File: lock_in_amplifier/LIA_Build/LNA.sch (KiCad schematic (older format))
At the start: 15 parts, among them J38 RF_Shield_One_Piece, U5 NC7SB3157, U6 NC7SB3157, U7 NC7SB3157, U8 AD8429

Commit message: power supply, amp chain first pass
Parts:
- removed C22: C, Capacitors_SMD:C_0805_HandSoldering, symbol C
- removed L8: L, Inductors_SMD:L_0805_HandSoldering, symbol L
- removed R16, R17, R18, R19, R20: R, symbol R
- added J24: LNA GAIN MODE, symbol Conn_01x02
- C20, C21: footprint Capacitors_SMD:C_0805_HandSoldering -> Capacitors_SMD:C_0805
- J38: footprint (none) -> footprints:SMS-201
- R21: value R -> 6.04; footprint (none) -> Resistors_SMD:R_0805
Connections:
- wire segments 27 -> 26
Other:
- note added: "A OR I SELECTION SWITCH"
- note added: "A/I OR A-B SELECTION SWITCH"
- note added: "AD8429 GAIN SELECTION VALUES (FROM DATASHEET)\n1x - open\n2x - 6.04k\n5x - 1.5k\n10x - 665 (2k||2k||2k)\n20x - 316\n50x - 121\n100x - 60.4 (121||121)\n1000x - 6.04"
- note added: "GAIN SELECTION SWITCH"
- note added: "GAIN SELECTION. INPUT LNA HAS 1 V/V (BUFFER MODE)\nOR 1000 V/V GAIN (LNA MODE).\nTHIS MINIMIZES "WEIRD" RESISTOR VALUE QUANTITIES.\nALSO REDUCES SIZE OF SWITCH BLOCK FOR EMI CONCERNS"
- note added: "INSTRUMENTATION AMPLIFIER SECTION\n"
- note added: "TRANSIMPEDANCE AMPLIFIER"
- note added: "◦ Transimpedance amp w/ switches for single ended, differential, and current inputs\n ◦ Nominal goal for 1 nV sensitivity with long enough time base; 1nV -> ~1V\n ▪ 1e9 v/v system gain.\n • Line filter at input - concerns with saturation\n\n"
- note removed: "A or I selection"
- note removed: "A/I or A-B selection"
- note removed: "INSTRUMENTATION AMPLIFIER SECTION\nNOTE: AD8428 (FIXED GAIN INST. AMP.) SUBSTITUTABLE BY REMOVING Rg"
- note removed: "TODO: line filter - 60Hz"
- note removed: "TODO: verify which resistors I have in stock\nminimaze part count\n1x - open\n2x - 6.04k\n5x - 1.5k\n10x - 665 (2k||2k||2k)\n20x - 316\n50x - 121\n100x - 60.4 (121||121)"
- note removed: "dip switch?"
- note removed: "gain selection block"
- note removed: "transimpedance amplifier"
- note removed: "◦ Transimpedance amp w/ switches for single ended, differential, and current inputs\n ▪ Component selection\n ▪ Switches - spdt\n ◦ Switched gain \n ▪ common numbers for measurement (1x one of the amps)\n ▪ Switch selection\n ▪ 2xN 100 mil header jumpers\n ▪ N pole N throw slide switch - $$$? Real estate?\n ▪ DIP\n • 2 amp cascade - LNA + “normal” amp\n ◦ Nominal goal for 1 nV sensitivity with lo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"
- moved on the sheet: C20, C21, J38, R21, U8

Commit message: initial transimpedance selection, lna refinement
amp overload led
switch comps added
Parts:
- removed J24: LNA GAIN MODE, symbol Conn_01x02
- removed U5, U6, U7: NC7SB3157, symbol NC7SB3157
- added C25, C27: 10pF, symbol C
- added C34, C35, C37, C38: 0.1u, Capacitors_SMD:C_0805, symbol C
- added C36, C39: C, symbol C
- added J17: RF_Shield_One_Piece, footprints:SMS-201, symbol RF_Shield_One_Piece
- added R46: 10k, symbol R
- added R47, R58: 100, symbol R
- added R48, R55: 1M, symbol R
- added R49, R50: 10M, symbol R
- added R56, R57: 0, symbol R
- added R59: R, symbol R
- added R60: 10, symbol R
- added S4: A / I SEL, symbol SPDT
- added S5: B SEL, symbol SPDT
- added S6: LNA GAIN SEL, symbol SPDT
- added U6: lmp7721, Housings_SSOP:MSOP-8-1EP_3x3mm_Pitch0.65mm, symbol lmp7721
- added U7: OP1177, Housings_SSOP:MSOP-8-1EP_3x3mm_Pitch0.65mm, symbol OP1177
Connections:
- wire segments 26 -> 78
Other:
- note added: "AD8429 GAIN SELECTION VALUES (FROM DATASHEET)\n1x - open\n2x - 6.04k\n5x - 1.5k\n10x - 665 (2k||2k||2k)\n20x - 316\n50x - 121\n100x - 60.4 (121||121)\n1000x - 6.04\nGAIN SELECTION. INPUT LNA HAS 1 V/V (BUFFER MODE)\nOR 1000 V/V GAIN (LNA MODE).\nTHIS MINIMIZES "WEIRD" RESISTOR VALUE QUANTITIES."
- note added: "CONSIDER 6.04 (OR 2X 6.04) FOR RG TO REDUCE PART COUNT"
- note added: "DETERMINE FEED BACK AND LOOP BW"
- note added: "DETERMINE FEEDBACK RESISTANCE\nDETERMINE LOOP BW"
- note added: "DETERMINE POTENTIAL FOR THIS CAN."
- note added: "DETERMINE Rgd VALUE"
- note added: "DNI"
- note added: "GAIN SELECTION SWITCH\nFULL OUTPUT OR DIV/1000\n10k || 1M = 9.901k"
- note added: "GUARD DRIVER"
- note added: "LAYOUT GUIDELINE: GUARD TRACE \nMUST SURROUND CURRENT INPUT TRACE\nREMOVE SOLDER MASK FROM INSIDE GUARD TRACE\nCAN SHOULD COMPOSE GUARD TRACE WHERE POSSIBLE"
- note added: "LAYOUT: \nPLACE GND/REF FB TERMINAL\nOUTSIDE GUARD AREA"
- note added: "LNA INSTRUMENTATION AMP"
- note added: "◦ Transimpedance amp w/ switches for single ended, differential, and current inputs\n ◦ Nominal goal for 1 nV sensitivity with long enough time base; 1nV -> ~1V\n ▪ 1e9 v/v system gain.\n • Line filter at output - concerns with saturation on high gain amp, not lna\n\n"
- note removed: "AD8429 GAIN SELECTION VALUES (FROM DATASHEET)\n1x - open\n2x - 6.04k\n5x - 1.5k\n10x - 665 (2k||2k||2k)\n20x - 316\n50x - 121\n100x - 60.4 (121||121)\n1000x - 6.04"
- note removed: "DNI - leave off unless neccesary\ncover input of LNA"
- note removed: "GAIN SELECTION SWITCH"
- note removed: "GAIN SELECTION. INPUT LNA HAS 1 V/V (BUFFER MODE)\nOR 1000 V/V GAIN (LNA MODE).\nTHIS MINIMIZES "WEIRD" RESISTOR VALUE QUANTITIES.\nALSO REDUCES SIZE OF SWITCH BLOCK FOR EMI CONCERNS"
- note removed: "INSTRUMENTATION AMPLIFIER SECTION\n"
- note removed: "◦ Transimpedance amp w/ switches for single ended, differential, and current inputs\n ◦ Nominal goal for 1 nV sensitivity with long enough time base; 1nV -> ~1V\n ▪ 1e9 v/v system gain.\n • Line filter at input - concerns with saturation\n\n"
- moved on the sheet: C20, C21, J38, R21, U8

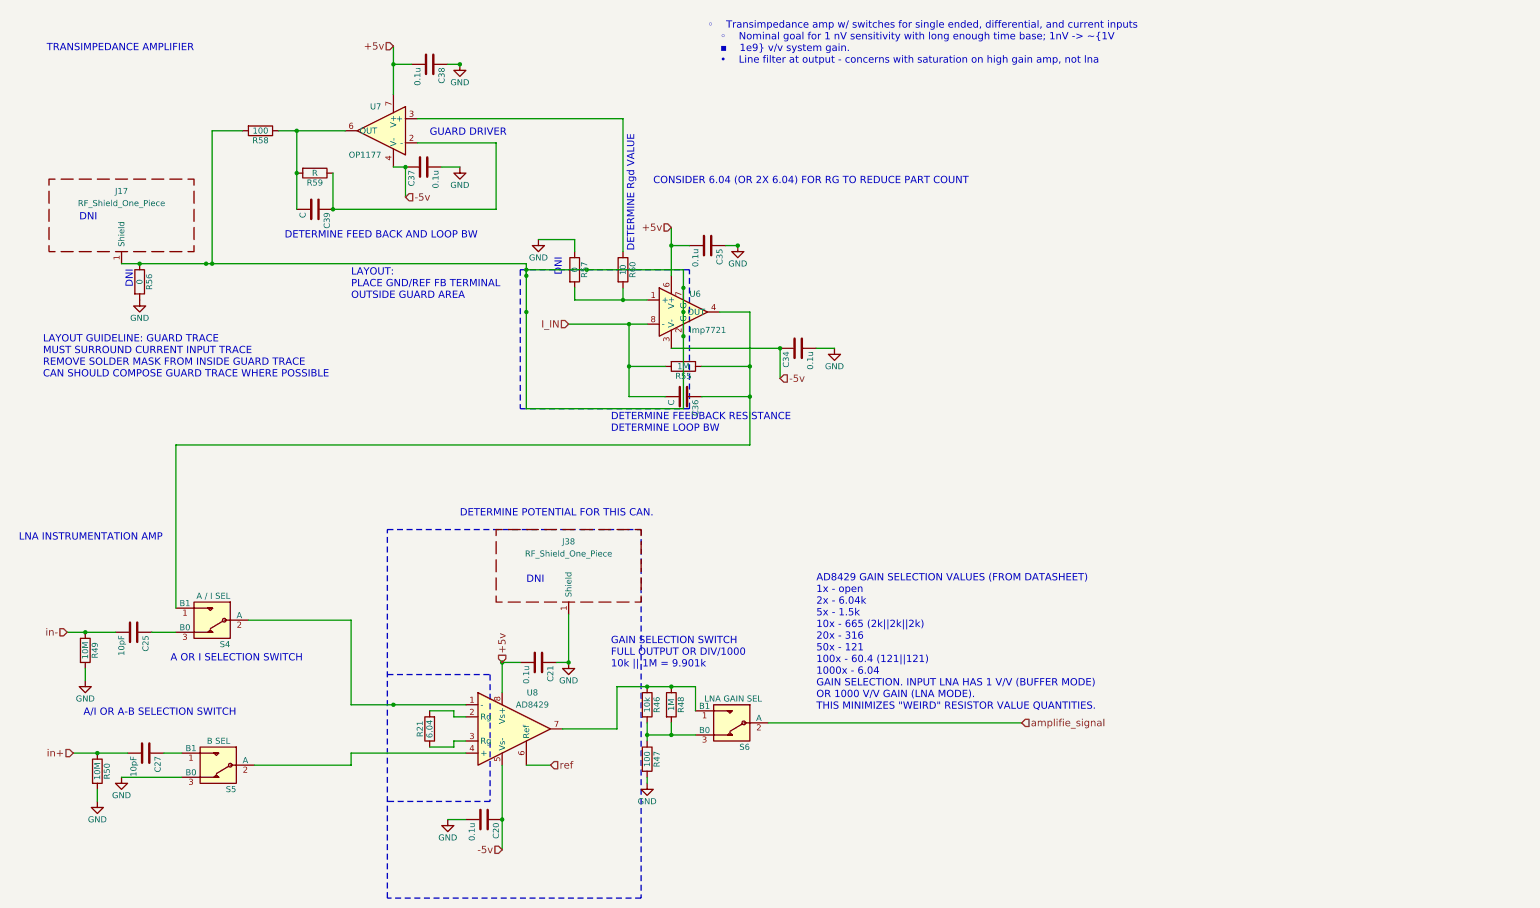
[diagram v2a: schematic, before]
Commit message: switch footprints, lm833 usage, pll investigation
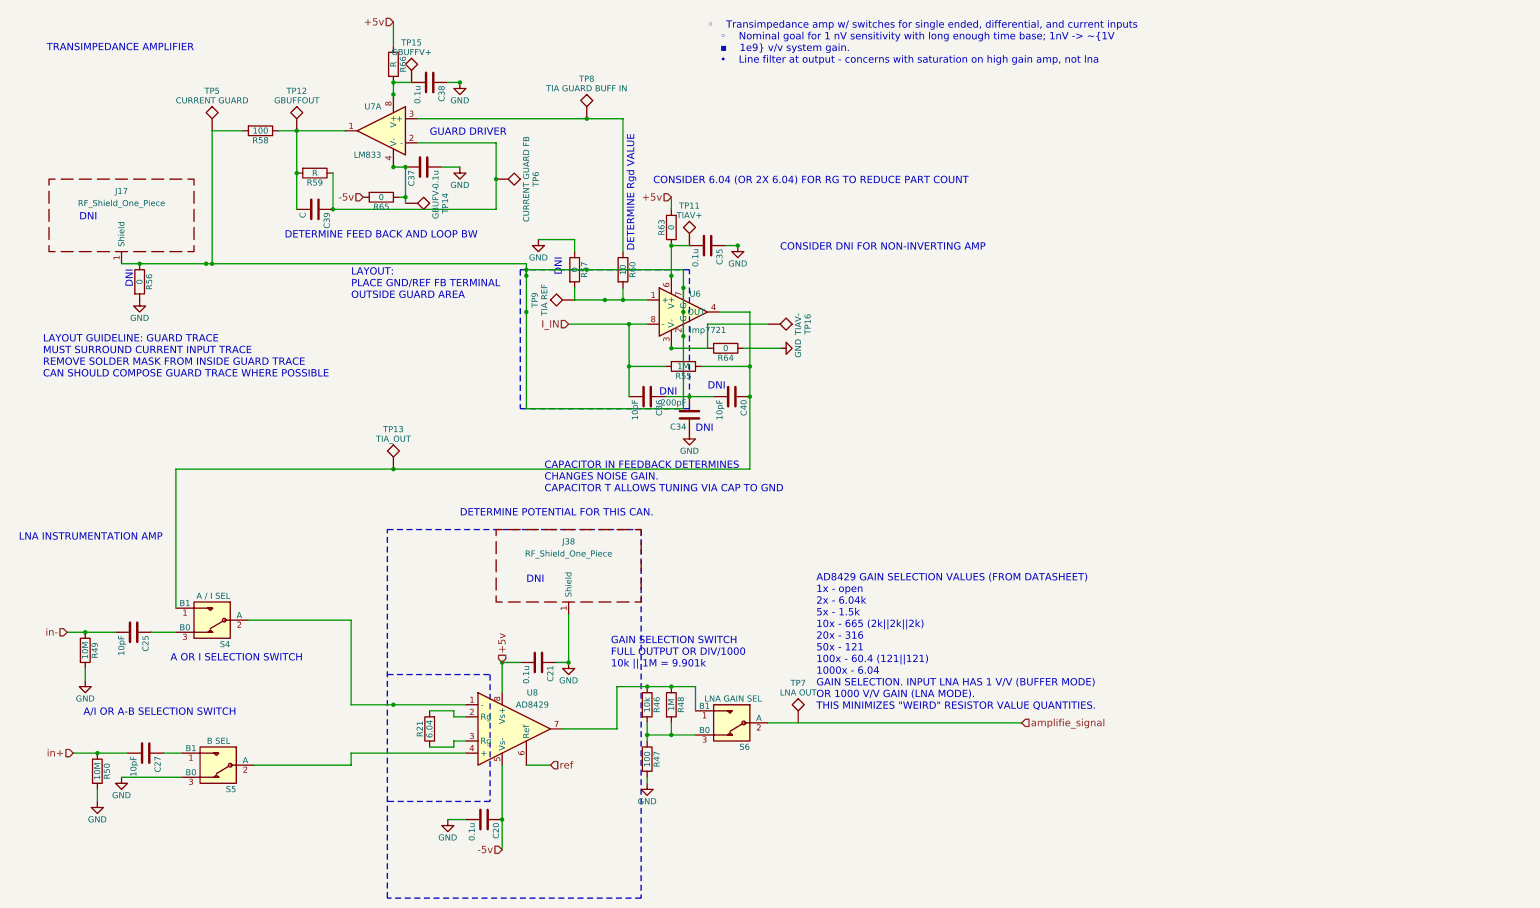
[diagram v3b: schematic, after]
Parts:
- removed U7: OP1177, Housings_SSOP:MSOP-8-1EP_3x3mm_Pitch0.65mm, symbol OP1177
- added C40: 10pF, symbol C
- added R63, R64, R65: 0, symbol R
- added R66: R, symbol R
- added TP11: TIAV+, symbol TEST
- added TP12: GBUFFOUT, symbol TEST
- added TP13: TIA_OUT, symbol TEST
- added TP14: GBUFV-, symbol TEST
- added TP15: GBUFFV+, symbol TEST
- added TP16: TIAV-, symbol TEST
- added TP5: CURRENT GUARD, symbol TEST
- added TP6: CURRENT GUARD FB, symbol TEST
- added TP7: LNA OUT, symbol TEST
- added TP8: TIA GUARD BUFF IN, symbol TEST
- added TP9: TIA REF, symbol TEST
- added U7: LM833, symbol LM833
- C34: value 0.1u -> 200pF; footprint Capacitors_SMD:C_0805 -> (none)
- C36: value C -> 10pF
- S4, S5, S6: footprint (none) -> footprints:SPDT_OS102011MS2QN1
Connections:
- net +5v: now also R63.2, R66.1; no longer C35.2, C38.2, U6.6 (V+)
- net -5v: now also R65.2; no longer C34.1, C37.1, U6.3 (V-)
- net GND: now also C34.1, R64.1; no longer C34.2
- net at R55.1, S4.1 (B1), U6.4 (OUT): now also C40.1, TP13.1; no longer C36.1
- net at J17.1 (Shield), R56.1, R58.2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: now also TP5.1
- net at C39.1, R59.1: now also TP6.1, U7.2 (-)
- net at R60.1: now also TP8.1, U7.3 (+)
- net at C39.2, R58.1, R59.2: now also TP12.1, U7.1
- net at R57.2, R60.2, U6.1 (+): now also TP9.1
- new net: C35.2, R63.1, TP11.1, U6.6 (V+)
- new net: C34.2, C36.1, C40.2
- new net: C38.2, R66.2, TP15.1, U7.8 (V+)
- new net: C37.1, R65.1, TP14.1, U7.4 (V-)
- new net: R64.2, TP16.1, U6.3 (V-)
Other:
- note added: "CAPACITOR IN FEEDBACK DETERMINES \nCHANGES NOISE GAIN.\nCAPACITOR T ALLOWS TUNING VIA CAP TO GND"
- note added: "CONSIDER DNI FOR NON-INVERTING AMP"
- note removed: "DETERMINE FEEDBACK RESISTANCE\nDETERMINE LOOP BW"
- moved on the sheet: C36, C38

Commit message: pll finalized - misc cleanup - review candidate
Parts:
- R60: value 10 -> 10K
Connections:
- net amplifie_signal: now also TP7.1
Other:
- note added: "◦ Transimpedance amp w/ switches for single ended, differential, and current inputs\n ◦ Nominal goal for 1 nV sensitivity with long enough time base; 1nV -> ~1V\n ▪ 1e9 v/v system gain.\n\n"
- note removed: "CONSIDER 6.04 (OR 2X 6.04) FOR RG TO REDUCE PART COUNT"
- note removed: "CONSIDER DNI FOR NON-INVERTING AMP"
- note removed: "DETERMINE POTENTIAL FOR THIS CAN."
- note removed: "DETERMINE Rgd VALUE"
- note removed: "◦ Transimpedance amp w/ switches for single ended, differential, and current inputs\n ◦ Nominal goal for 1 nV sensitivity with long enough time base; 1nV -> ~1V\n ▪ 1e9 v/v system gain.\n • Line filter at output - concerns with saturation on high gain amp, not lna\n\n"
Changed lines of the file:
@@
 $EndComp
 $Comp
-L GND #PWR067
+L GND #PWR073
 U 1 1 5A1C75B0
 P 4100 7200
-F 0 "#PWR067" H 4100 6950 50  0001 C CNN
+F 0 "#PWR073" H 4100 6950 50  0001 C CNN
 F 1 "GND" H 4100 7050 50  0000 C CNN
 F 2 "" H 4100 7200 50  0001 C CNN
@@
 $EndComp
 $Comp
-L GND #PWR068
+L GND #PWR074
 U 1 1 5A1C75B6
 P 5100 5900
-F 0 "#PWR068" H 5100 5650 50  0001 C CNN
+F 0 "#PWR074" H 5100 5650 50  0001 C CNN
 F 1 "GND" H 5100 5750 50  0000 C CNN
 F 2 "" H 5100 5900 50  0001 C CNN
@@
 +5v
 Text Notes 6250 1050 0    60   ~ 0
-	◦	Transimpedance amp w/ switches for single ended, differential, and current inputs\n	◦	Nominal goal for 1 nV sensitivity with long enough time base; 1nV -> ~1V\n	▪	1e9 v/v system gain.\n	•	Line filter at output - concerns with saturation on high gain amp, not lna\n\n
+	◦	Transimpedance amp w/ switches for single ended, differential, and current inputs\n	◦	Nominal goal for 1 nV sensitivity with long enough time base; 1nV -> ~1V\n	▪	1e9 v/v system gain.\n\n
 $Comp
 L R R21
@@
 TRANSIMPEDANCE AMPLIFIER
 $Comp
-L GND #PWR069
+L GND #PWR075
 U 1 1 5A1F5BDB
 P 1400 6850
-F 0 "#PWR069" H 1400 6600 50  0001 C CNN
+F 0 "#PWR075" H 1400 6600 50  0001 C CNN
 F 1 "GND" H 1400 6700 50  0000 C CNN
 F 2 "" H 1400 6850 50  0001 C CNN
@@
 Text Notes 5450 5950 0    60   ~ 0
 GAIN SELECTION SWITCH\nFULL OUTPUT OR DIV/1000\n10k || 1M = 9.901k
-Text Notes 4200 4700 0    60   ~ 0
-DETERMINE POTENTIAL FOR THIS CAN.
 $Comp
 L R R46
@@
 $EndComp
 $Comp
-L GND #PWR070
+L GND #PWR076
 U 1 1 5A276A01
 P 5750 6900
-F 0 "#PWR070" H 5750 6650 50  0001 C CNN
+F 0 "#PWR076" H 5750 6650 50  0001 C CNN
 F 1 "GND" H 5750 6750 50  0000 C CNN
 F 2 "" H 5750 6900 50  0001 C CNN
@@
 $EndComp
 $Comp
-L GND #PWR071
+L GND #PWR077
 U 1 1 5A277FAE
 P 1100 6050
-F 0 "#PWR071" H 1100 5800 50  0001 C CNN
+F 0 "#PWR077" H 1100 5800 50  0001 C CNN
 F 1 "GND" H 1100 5900 50  0000 C CNN
 F 2 "" H 1100 6050 50  0001 C CNN
@@
 $EndComp
 $Comp
-L GND #PWR072
+L GND #PWR078
 U 1 1 5A277FE0
 P 1200 7050
-F 0 "#PWR072" H 1200 6800 50  0001 C CNN
+F 0 "#PWR078" H 1200 6800 50  0001 C CNN
 F 1 "GND" H 1200 6900 50  0000 C CNN
 F 2 "" H 1200 7050 50  0001 C CNN
@@
 $EndComp
 $Comp
-L GND #PWR073
+L GND #PWR079
 U 1 1 5A21D13B
 P 6850 3300
-F 0 "#PWR073" H 6850 3050 50  0001 C CNN
+F 0 "#PWR079" H 6850 3050 50  0001 C CNN
 F 1 "GND" H 6850 3150 50  0000 C CNN
 F 2 "" H 6850 3300 50  0001 C CNN
@@
 $EndComp
 $Comp
-L GND #PWR074
+L GND #PWR080
 U 1 1 5A21D39E
 P 6500 2450
-F 0 "#PWR074" H 6500 2200 50  0001 C CNN
+F 0 "#PWR080" H 6500 2200 50  0001 C CNN
 F 1 "GND" H 6500 2300 50  0000 C CNN
 F 2 "" H 6500 2450 50  0001 C CNN
@@
 GUARD DRIVER
 $Comp
-L GND #PWR075
+L GND #PWR081
 U 1 1 5A220C69
 P 4200 1100
-F 0 "#PWR075" H 4200 850 50  0001 C CNN
+F 0 "#PWR081" H 4200 850 50  0001 C CNN
 F 1 "GND" H 4200 950 50  0000 C CNN
 F 2 "" H 4200 1100 50  0001 C CNN
@@
 +5v
 $Comp
-L GND #PWR076
+L GND #PWR082
 U 1 1 5A220E76
 P 4200 1800
-F 0 "#PWR076" H 4200 1550 50  0001 C CNN
+F 0 "#PWR082" H 4200 1550 50  0001 C CNN
 F 1 "GND" H 4200 1650 50  0000 C CNN
 F 2 "" H 4200 1800 50  0001 C CNN
@@
 $EndComp
 $Comp
-L GND #PWR077
+L GND #PWR083
 U 1 1 5A221F33
 P 1550 2900
-F 0 "#PWR077" H 1550 2650 50  0001 C CNN
+F 0 "#PWR083" H 1550 2650 50  0001 C CNN
 F 1 "GND" H 1550 2750 50  0000 C CNN
 F 2 "" H 1550 2900 50  0001 C CNN
@@
 DNI
 $Comp
-L GND #PWR078
+L GND #PWR084
 U 1 1 5A2235D5
 P 4850 2400
-F 0 "#PWR078" H 4850 2150 50  0001 C CNN
+F 0 "#PWR084" H 4850 2150 50  0001 C CNN
 F 1 "GND" H 4850 2250 50  0000 C CNN
 F 2 "" H 4850 2400 50  0001 C CNN
@@
 P 5550 2650
 F 0 "R60" V 5630 2650 50  0000 C CNN
-F 1 "10" V 5550 2650 50  0000 C CNN
+F 1 "10K" V 5550 2650 50  0000 C CNN
 F 2 "" V 5480 2650 50  0001 C CNN
 F 3 "" H 5550 2650 50  0001 C CNN
@@
 	1    0    0    -1
 $EndComp
-Text Notes 5650 2500 1    60   ~ 0
-DETERMINE Rgd VALUE
-Text Notes 5800 1950 0    60   ~ 0
-CONSIDER 6.04 (OR 2X 6.04) FOR RG TO REDUCE PART COUNT
 Text Notes 5850 3700 0    60   ~ 0
 DNI
@@
 	1    0    0    -1
 $EndComp
-Text Notes 6850 2500 0    60   ~ 0
-CONSIDER DNI FOR NON-INVERTING AMP
 $Comp
 L TEST TP6
@@
 DNI
 $Comp
-L GND #PWR079
+L GND #PWR085
 U 1 1 5A2424BB
 P 6100 4000
-F 0 "#PWR079" H 6100 3750 50  0001 C CNN
+F 0 "#PWR085" H 6100 3750 50  0001 C CNN
 F 1 "GND" H 6100 3850 50  0000 C CNN
 F 2 "" H 6100 4000 50  0001 C CNN
@@
 	-1   0    0    -1
 $EndComp
+Connection ~ 7000 6400
+Connection ~ 3400 2050
+$Comp
+L PWR_FLAG #FLG086
+U 1 1 5A2D348D
+P 3650 1100
+F 0 "#FLG086" H 3650 1175 50  0001 C CNN
+F 1 "PWR_FLAG" H 3650 1250 50  0000 C CNN
+F 2 "" H 3650 1100 50  0001 C CNN
+F 3 "" H 3650 1100 50  0001 C CNN
+	1    3650 1100
+	0    -1   -1   0
+$EndComp
+$Comp
+L PWR_FLAG #FLG087
+U 1 1 5A2D35B5
+P 3650 1800
+F 0 "#FLG087" H 3650 1875 50  0001 C CNN
+F 1 "PWR_FLAG" H 3650 1950 50  0000 C CNN
+F 2 "" H 3650 1800 50  0001 C CNN
+F 3 "" H 3650 1800 50  0001 C CNN
+	1    3650 1800
+	0    -1   -1   0
+$EndComp
+$Comp
+L PWR_FLAG #FLG088
+U 1 1 5A2D36AF
+P 5950 2450
+F 0 "#FLG088" H 5950 2525 50  0001 C CNN
+F 1 "PWR_FLAG" H 5950 2600 50  0000 C CNN
+F 2 "" H 5950 2450 50  0001 C CNN
+F 3 "" H 5950 2450 50  0001 C CNN
+	1    5950 2450
+	0    -1   -1   0
+$EndComp
+$Comp
+L PWR_FLAG #FLG089
+U 1 1 5A2D374D
+P 5950 3300
+F 0 "#FLG089" H 5950 3375 50  0001 C CNN
+F 1 "PWR_FLAG" H 5950 3450 50  0000 C CNN
+F 2 "" H 5950 3300 50  0001 C CNN
+F 3 "" H 5950 3300 50  0001 C CNN
+	1    5950 3300
+	0    -1   -1   0
+$EndComp
 $EndSCHEMATC
